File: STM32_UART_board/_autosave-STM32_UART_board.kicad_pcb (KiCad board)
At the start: 2 copper layers, 47.5 x 42 mm, 33 parts, among them J1 SWD, J2 Scooter, Q1 AO4612_C4748739, SW1 SW_Push, SW2 SW_Push, U1 BAS70-05, U2 LM2574HVM-5, U3 AZ1117-3.3, U4 STM32C011F6Px

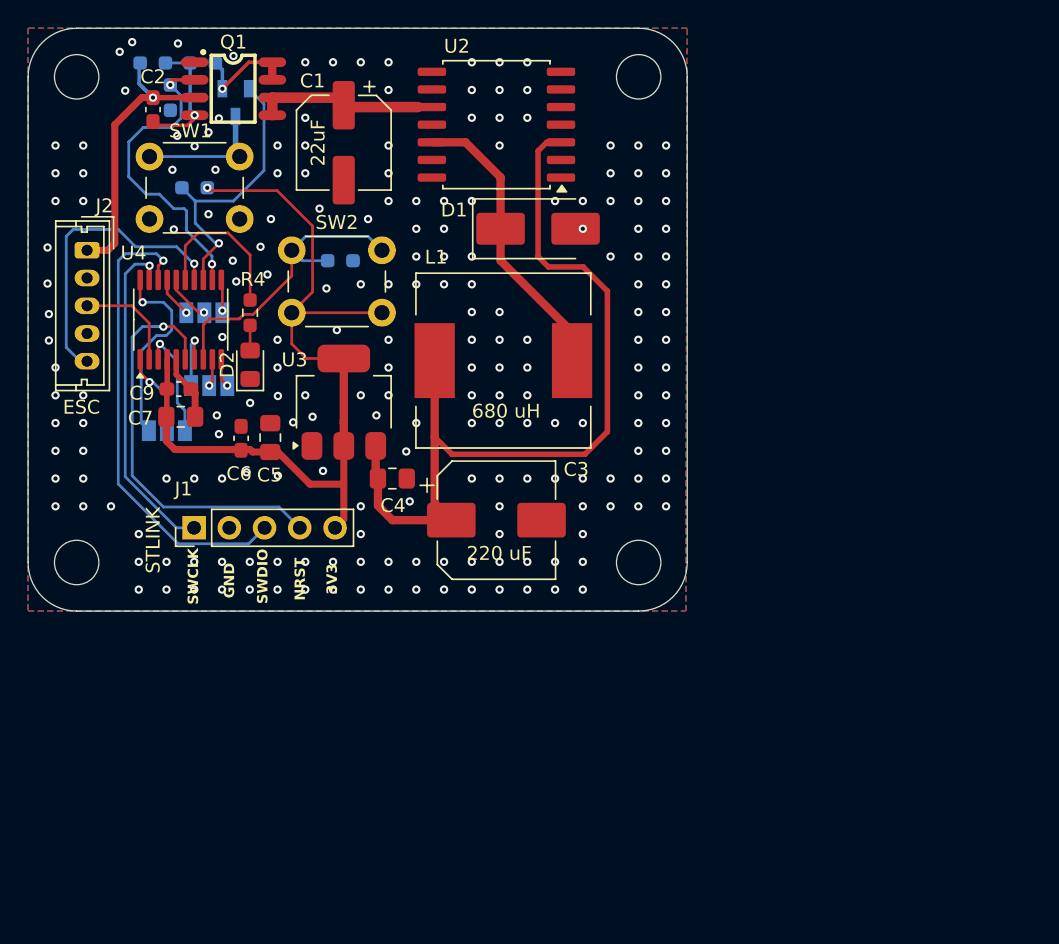
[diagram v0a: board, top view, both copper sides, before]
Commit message: PCB with swapped RX TX | initial code fot STM32C011
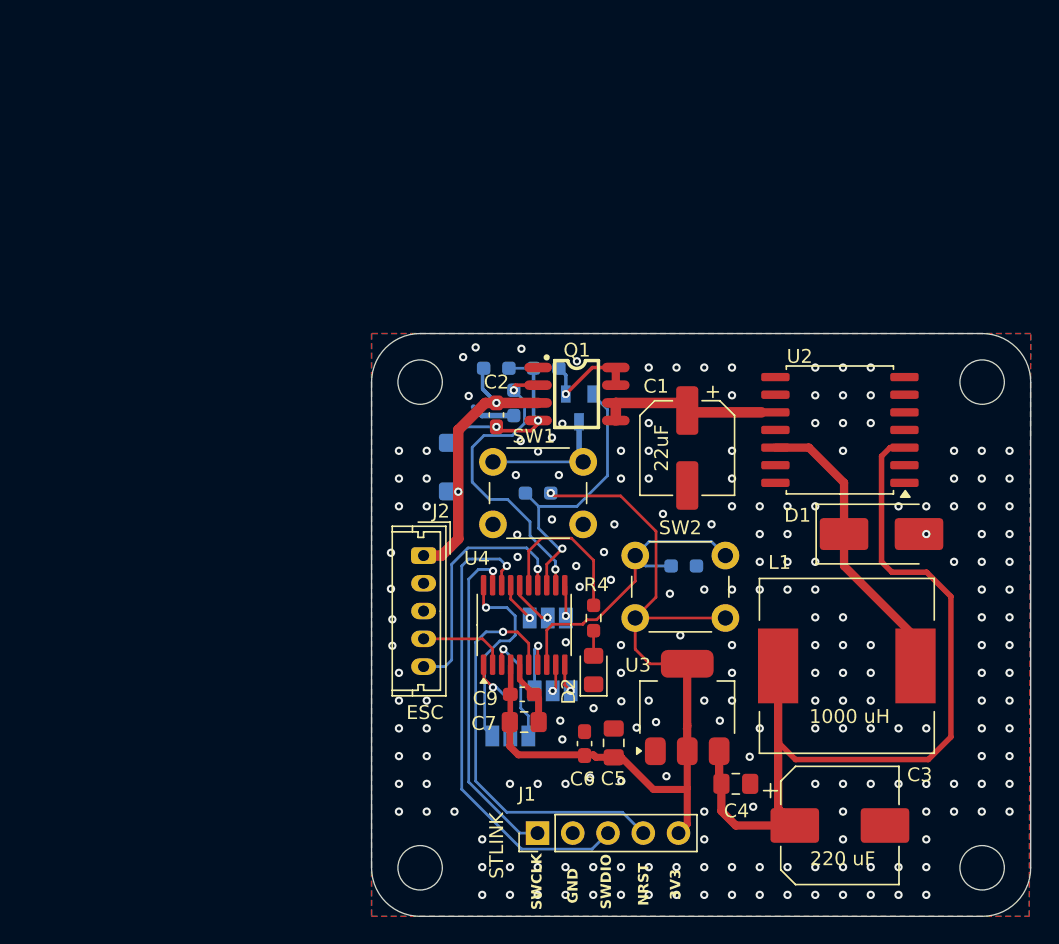
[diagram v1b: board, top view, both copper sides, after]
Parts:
- added D3: BZV55B15, Diode_SMD:D_MiniMELF, B.Cu at (94.0, 74.1)
- L1: value 680 uH -> 1000 uH
- moved C1 33.1 mm to (111.0, 72.8)
- moved C2 33.1 mm to (97.2, 70.4)
- moved C3 33.1 mm to (122.0, 100.0)
- moved C4 33.1 mm to (114.5, 97.0)
- moved C5 33.1 mm to (105.7, 94.0)
- moved C6 33.1 mm to (103.6, 94.0)
- moved C7 33.1 mm to (99.2, 92.5)
- moved C9 33.1 mm to (99.1, 90.5)
- moved D1 33.1 mm to (125.0, 79.0)
- moved D2 33.1 mm to (104.2, 88.8)
- moved H1 33.1 mm to (91.8, 103.0)
- moved H2 33.1 mm to (132.2, 103.0)
- moved H3 33.1 mm to (91.8, 68.0)
- moved H4 33.1 mm to (132.2, 68.0)
- moved J1 33.1 mm to (100.2, 100.5)
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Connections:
- J2 pad 3: /PC14 -> /SCOOTER_TX
- J2 pad 4: /SCOOTER_TX -> /PC14
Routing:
- net BATT+: track 21.0 -> 26.9 mm, vias 1 -> 2
- net /Q1_G1: track 9.23 -> 13.0 mm, vias 1 -> 2
- net /EN: track 21.5 -> 18.0 mm
- net GND: track 4.98 -> 8.13 mm, vias 203 -> 204
- net /PC14: track 7.61 -> 6.41 mm
